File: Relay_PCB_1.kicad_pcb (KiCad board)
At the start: 2 copper layers, 58.4 x 55.9 mm, 1 part

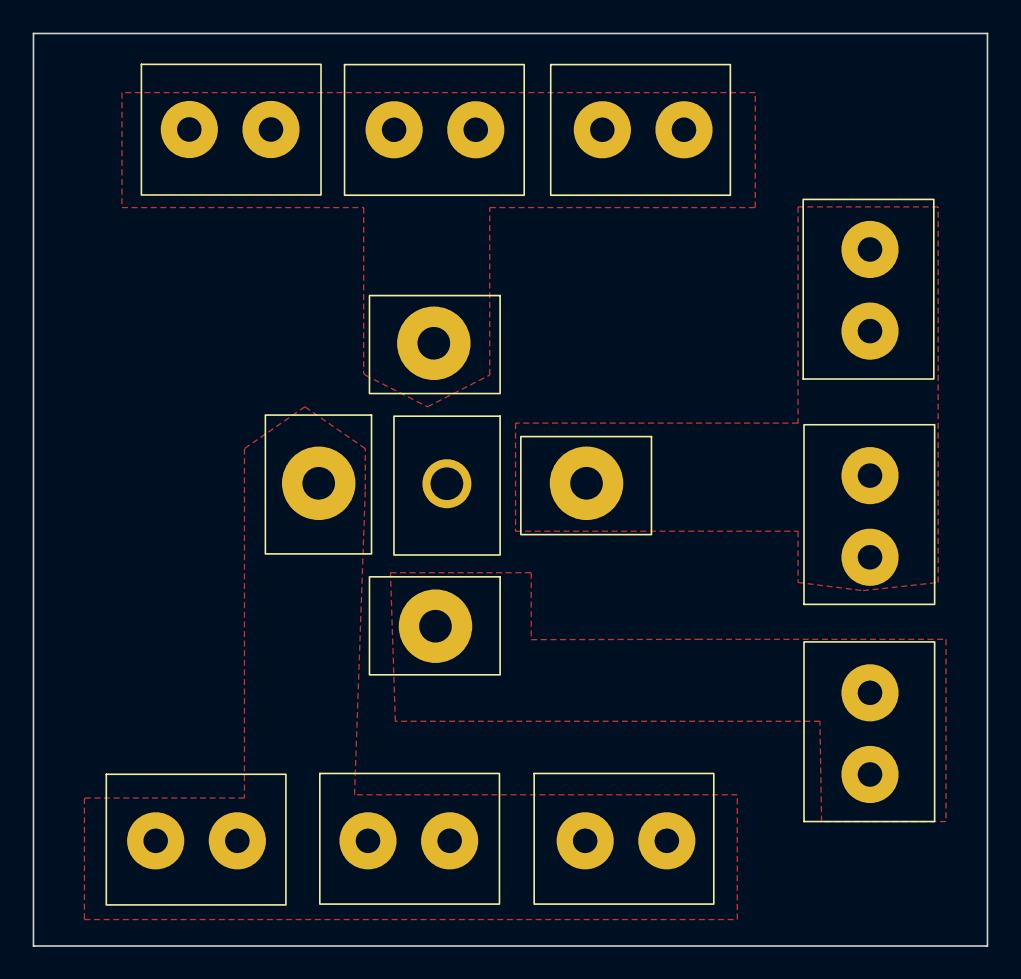
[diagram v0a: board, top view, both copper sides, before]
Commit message: fixed relay pin orientations
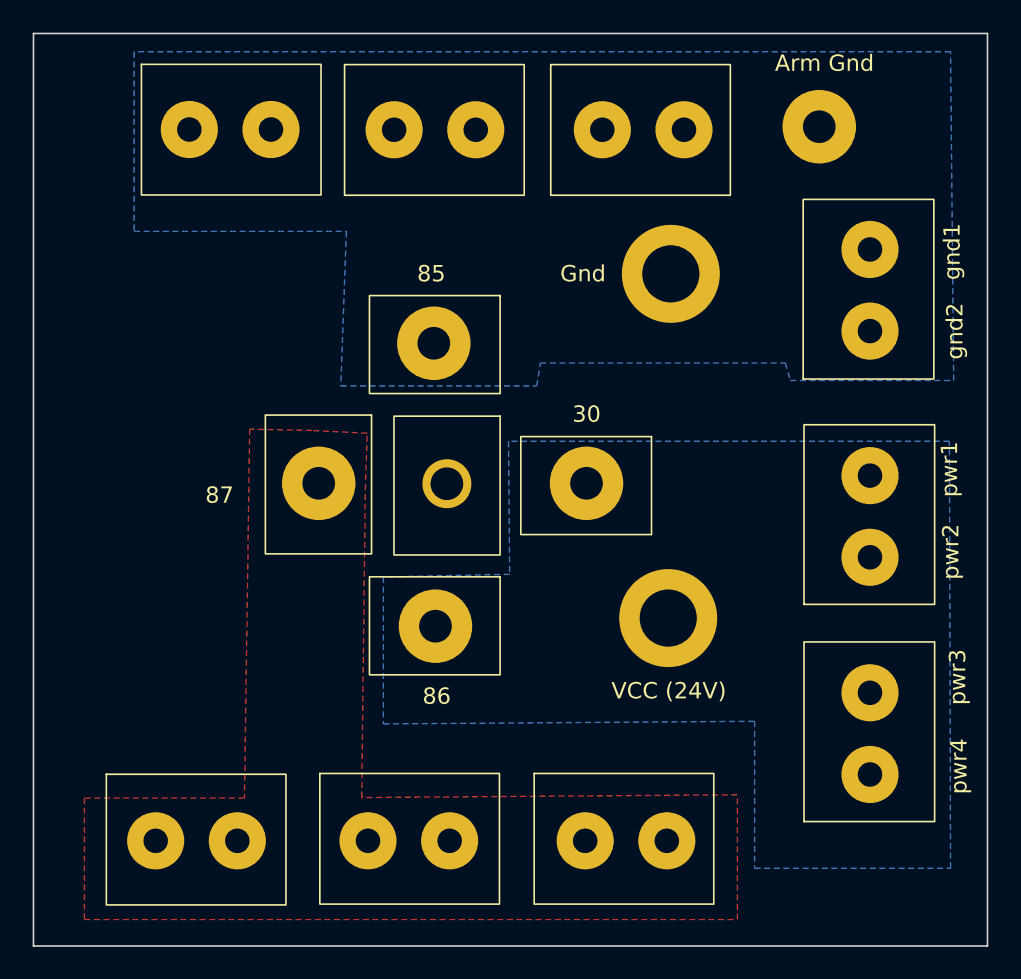
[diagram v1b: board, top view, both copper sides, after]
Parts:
- added ?: , , F.Cu at (165.0, 61.6)
- added ?: , , F.Cu at (155.9, 70.6)
- added ?: , , F.Cu at (155.7, 91.7)
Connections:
- ? pad 1: gnd -> pwr
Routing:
- net pwr: track 0.00 -> 0.61 mm
- net gnd: track 0.61 -> 0.00 mm
- added copper zone on B.Cu, net gnd
- added copper zone on B.Cu, net pwr
- removed copper zone on F.Cu, net gnd
- removed copper zone on F.Cu, net negative_motors
- removed copper zone on F.Cu, net pwr
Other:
- board text added: "30"
- board text added: "85"
- board text added: "86"
- board text added: "87"
- board text added: "Arm Gnd"
- board text added: "Gnd"
- board text added: "VCC (24V)"
- board text added: "gnd1"
- board text added: "gnd2"
- board text added: "pwr1"
- board text added: "pwr2"
- board text added: "pwr3"
- board text added: "pwr4"
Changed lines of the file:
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@@
   (net 0 "")
   (net 1 "positive_motors")
-  (net 2 "negative_motors")
-  (net 3 "pwr")
-  (net 4 "gnd")
+  (net 2 "pwr")
+  (net 3 "gnd")
+  (footprint "" (layer "F.Cu")
+    (at 164.96 61.59)
+    (fp_text reference "" (at 0 0) (layer "F.SilkS")
+        (effects (font (size 1.27 1.27) (thickness 0.15)))
+    )
+    (fp_text value "" (at 0 0) (layer "F.SilkS")
+        (effects (font (size 1.27 1.27) (thickness 0.15)))
+    )
+    (pad "2" thru_hole circle (at 0 0) (size 4.5 4.5) (drill 2) (layers "*.Cu" "*.Mask")
+      (net 3 "gnd"))
+  )
+  (footprint "" (layer "F.Cu")
+    (at 155.87 70.6)
+    (fp_text reference "" (at 0 0) (layer "F.SilkS")
+        (effects (font (size 1.27 1.27) (thickness 0.15)))
+    )
+    (fp_text value "" (at 0 0) (layer "F.SilkS")
+        (effects (font (size 1.27 1.27) (thickness 0.15)))
+    )
+    (pad "2" thru_hole circle (at 0 0) (size 6 6) (drill 3.5) (layers "*.Cu" "*.Mask")
+      (net 3 "gnd"))
+  )
   (footprint "clipboard:3956bf9f-648b-47b4-8fb4-f867ac44dcf9" (layer "F.Cu")
     (at 152.4 109.22)
@@
       (net 1 "positive_motors"))
     (pad "1" thru_hole circle (at -26.016 -47.46) (size 3.5 3.5) (drill 1.5) (layers "*.Cu" "*.Mask")
-      (net 2 "negative_motors"))
+      (net 3 "gnd"))
     (pad "1" thru_hole circle (at -23.076 -3.9) (size 3.5 3.5) (drill 1.5) (layers "*.Cu" "*.Mask")
       (net 1 "positive_motors"))
     (pad "1" thru_hole circle (at -21.016 -47.46) (size 3.5 3.5) (drill 1.5) (layers "*.Cu" "*.Mask")
-      (net 2 "negative_motors"))
+      (net 3 "gnd"))
     (pad "1" thru_hole circle (at -15.075 -3.9) (size 3.5 3.5) (drill 1.5) (layers "*.Cu" "*.Mask")
       (net 1 "positive_motors"))
     (pad "1" thru_hole circle (at -13.475 -47.444) (size 3.5 3.5) (drill 1.5) (layers "*.Cu" "*.Mask")
-      (net 2 "negative_motors"))
+      (net 3 "gnd"))
     (pad "1" thru_hole circle (at -10.075 -3.9) (size 3.5 3.5) (drill 1.5) (layers "*.Cu" "*.Mask")
       (net 1 "positive_motors"))
     (pad "1" thru_hole circle (at -8.475 -47.444) (size 3.5 3.5) (drill 1.5) (layers "*.Cu" "*.Mask")
-      (net 2 "negative_motors"))
+      (net 3 "gnd"))
     (pad "1" thru_hole circle (at -1.775 -3.9) (size 3.5 3.5) (drill 1.5) (layers "*.Cu" "*.Mask")
       (net 1 "positive_motors"))
     (pad "1" thru_hole circle (at -0.725 -47.444) (size 3.5 3.5) (drill 1.5) (layers "*.Cu" "*.Mask")
-      (net 2 "negative_motors"))
+      (net 3 "gnd"))
     (pad "1" thru_hole circle (at 3.225 -3.9) (size 3.5 3.5) (drill 1.5) (layers "*.Cu" "*.Mask")
       (net 1 "positive_motors"))
     (pad "1" thru_hole circle (at 4.275 -47.444) (size 3.5 3.5) (drill 1.5) (layers "*.Cu" "*.Mask")
-      (net 2 "negative_motors"))
+      (net 3 "gnd"))
     (pad "1" thru_hole circle (at 15.667 -40.114) (size 3.5 3.5) (drill 1.5) (layers "*.Cu" "*.Mask")
-      (net 3 "pwr"))
+      (net 3 "gnd"))
     (pad "1" thru_hole circle (at 15.667 -35.114) (size 3.5 3.5) (drill 1.5) (layers "*.Cu" "*.Mask")
-      (net 3 "pwr"))
+      (net 3 "gnd"))
     (pad "1" thru_hole circle (at 15.667 -26.264) (size 3.5 3.5) (drill 1.5) (layers "*.Cu" "*.Mask")
-      (net 3 "pwr"))
+      (net 2 "pwr"))
     (pad "1" thru_hole circle (at 15.667 -21.264) (size 3.5 3.5) (drill 1.5) (layers "*.Cu" "*.Mask")
-      (net 3 "pwr"))
+      (net 2 "pwr"))
     (pad "1" thru_hole circle (at 15.667 -12.964) (size 3.5 3.5) (drill 1.5) (layers "*.Cu" "*.Mask")
-      (net 4 "gnd"))
+      (net 2 "pwr"))
     (pad "1" thru_hole circle (at 15.667 -7.964) (size 3.5 3.5) (drill 1.5) (layers "*.Cu" "*.Mask")
-      (net 4 "gnd"))
+      (net 2 "pwr"))
     (pad "2" thru_hole circle (at -18.093 -25.794) (size 4.5 4.5) (drill 2) (layers "*.Cu" "*.Mask")
       (net 1 "positive_motors"))
     (pad "2" thru_hole circle (at -11.043 -34.369) (size 4.5 4.5) (drill 2) (layers "*.Cu" "*.Mask")
-      (net 2 "negative_motors"))
+      (net 3 "gnd"))
     (pad "2" thru_hole circle (at -10.943 -17.044) (size 4.5 4.5) (drill 2) (layers "*.Cu" "*.Mask")
-      (net 4 "gnd"))
+      (net 2 "pwr"))
     (pad "2" thru_hole circle (at -10.243 -25.769) (size 3 3) (drill 2) (layers "*.Cu" "*.Mask"))
     (pad "2" thru_hole circle (at -1.693 -25.794) (size 4.5 4.5) (drill 2) (layers "*.Cu" "*.Mask")
-      (net 3 "pwr"))
+      (net 2 "pwr"))
+  )
+  (footprint "" (layer "F.Cu")
+    (at 155.71 91.68)
+    (fp_text reference "" (at 0 0) (layer "F.SilkS")
+        (effects (font (size 1.27 1.27) (thickness 0.15)))
+    )
+    (fp_text value "" (at 0 0) (layer "F.SilkS")
+        (effects (font (size 1.27 1.27) (thickness 0.15)))
+    )
+    (pad "2" thru_hole circle (at 0 0) (size 6 6) (drill 3.5) (layers "*.Cu" "*.Mask")
+      (net 2 "pwr"))
   )
   (gr_rect (start 116.84 55.88) (end 175.26 111.76)
     (stroke (width 0.1) (type default)) (fill none) (layer "Edge.Cuts"))
+  (gr_text "85" (at 140.33 71.18) (layer "F.SilkS")
+    (effects (font (size 1 1) (thickness 0.1)) (justify left bottom))
+  )
+  (gr_text "30\n" (at 149.84 79.78) (layer "F.SilkS")
+    (effects (font (size 1 1) (thickness 0.1)) (justify left bottom))
+  )
+  (gr_text "86" (at 140.66 97.05) (layer "F.SilkS")
+    (effects (font (size 1 1) (thickness 0.1)) (justify left bottom))
+  )
+  (gr_text "pwr4\n" (at 174.1 102.47 90) (layer "F.SilkS")
+    (effects (font (size 1 1) (thickness 0.1)) (justify left bottom))
+  )
+  (gr_text "gnd2\n" (at 173.85 75.85 90) (layer "F.SilkS")
+    (effects (font (size 1 1) (thickness 0.1)) (justify left bottom))
+  )
+  (gr_text "gnd1" (at 173.68 70.98 90) (layer "F.SilkS")
+    (effects (font (size 1 1) (thickness 0.1)) (justify left bottom))
+  )
+  (gr_text "pwr1" (at 173.52 84.28 90) (layer "F.SilkS")
+    (effects (font (size 1 1) (thickness 0.1)) (justify left bottom))
+  )
+  (gr_text "VCC (24V)" (at 152.23 96.72) (layer "F.SilkS")
+    (effects (font (size 1 1) (thickness 0.1)) (justify left bottom))
+  )
+  (gr_text "Gnd" (at 149.09 71.18) (layer "F.SilkS")
+    (effects (font (size 1 1) (thickness 0.1)) (justify left bottom))
+  )
+  (gr_text "Arm Gnd" (at 162.24 58.29) (layer "F.SilkS")
+    (effects (font (size 1 1) (thickness 0.1)) (justify left bottom))
+  )
+  (gr_text "pwr3\n" (at 174.02 97.01 90) (layer "F.SilkS")
+    (effects (font (size 1 1) (thickness 0.1)) (justify left bottom))
+  )
+  (gr_text "pwr2\n" (at 173.6 89.33 90) (layer "F.SilkS")
+    (effects (font (size 1 1) (thickness 0.1)) (justify left bottom))
+  )
+  (gr_text "87" (at 127.36 84.74) (layer "F.SilkS")
+    (effects (font (size 1 1) (thickness 0.1)) (justify left bottom))
+  )
   (segment (start 134.3 83.433) (end 134.307 83.426) (width 0) (layer "F.Cu") (net 1))
   (segment (start 133.7 84.033) (end 134.307 83.426) (width 0) (layer "F.Cu") (net 1))
-  (segment (start 141.891 92.61) (end 141.457 92.176) (width 0.2) (layer "F.Cu") (net 4))
+  (segment (start 141.891 92.61) (end 141.457 92.176) (width 0.2) (layer "F.Cu") (net 2))
   (zone (net 1) (net_name "positive_motors") (layer "F.Cu") (hatch edge 0.5)
     (priority 2)
@@
     (polygon
       (pts
-        (xy 133.46 78.74)
-        (xy 129.76 81.3)
+        (xy 133.89 80.19)
+        (xy 130.08 80.11)
         (xy 129.76 102.7)
         (xy 119.96 102.7)
@@
         (xy 159.94 110.14)
         (xy 159.94 102.5)
-        (xy 136.5 102.5)
+        (xy 136.94 102.67)
         (xy 137.16 83.82)
-        (xy 137.16 81.3)
+        (xy 137.28 80.36)
       )
     )
   )
-  (zone (net 3) (net_name "pwr") (layer "F.Cu") (hatch edge 0.5)
-    (priority 1)
+  (zone (net 3) (net_name "gnd") (layer "B.Cu") (hatch edge 0.5)
     (connect_pads yes (clearance 0.5))
-    (min_thickness 0.4) (filled_areas_thickness no)
+    (min_thickness 0.3) (filled_areas_thickness no)
     (fill yes (thermal_gap 0.5) (thermal_bridge_width 0.5))
     (polygon
       (pts
-        (xy 146.36 79.74)
-        (xy 146.36 86.36)
-        (xy 163.66 86.36)
-        (xy 163.66 89.5)
-        (xy 167.64 90)
-        (xy 172.24 89.5)
-        (xy 172.24 66.5)
-        (xy 163.66 66.5)
-        (xy 163.66 79.74)
+        (xy 123 57)
+        (xy 123 68)
+        (xy 136 68)
+        (xy 135.66 77.46)
+        (xy 147.66 77.46)
+        (xy 147.88 76.06)
+        (xy 162.88 76.06)
+        (xy 163.19 77.13)
+        (xy 173.19 77.13)
+        (xy 173 57)
       )
     )
   )
-  (zone (net 4) (net_name "gnd") (layer "F.Cu") (hatch edge 0.5)
-    (priority 3)
+  (zone (net 2) (net_name "pwr") (layer "B.Cu") (hatch edge 0.5)
+    (priority 1)
     (connect_pads yes (clearance 0.5))
-    (min_thickness 0.25) (filled_areas_thickness no)
+    (min_thickness 0.3) (filled_areas_thickness no)
     (fill yes (thermal_gap 0.5) (thermal_bridge_width 0.5))
     (polygon
       (pts
-        (xy 147.32 88.9)
-        (xy 147.32 93)
-        (xy 157.48 92.98)
-        (xy 172.72 92.98)
-        (xy 172.72 104.14)
-        (xy 165.1 104.14)
-        (xy 165 98)
-        (xy 139 98)
-        (xy 138.7 88.9)
+        (xy 138.27 89.16)
+        (xy 138.27 98.16)
+        (xy 161 98)
+        (xy 161 107)
+        (xy 173 107)
+        (xy 172.93 80.85)
+        (xy 145.93 80.85)
+        (xy 146 89)
       )
     )
-  )
-  (zone (net 2) (net_name "negative_motors") (layer "F.Cu") (hatch edge 0.5)
-    (connect_pads yes (clearance 0.5))
-    (min_thickness 0.4) (filled_areas_thickness no)
-    (fill yes (thermal_gap 0.5) (thermal_bridge_width 0.5))
-    (polygon
-      (pts
-        (xy 137.16 76.8)
-        (xy 140.97 78.74)
-        (xy 144.78 76.8)
-        (xy 144.78 66.54)
-        (xy 161.04 66.54)
-        (xy 161.04 59.5)
-        (xy 122.26 59.5)
-        (xy 122.26 66.54)
-        (xy 137.06 66.54)
-        (xy 137.06 76.7)
-      )
-    )
